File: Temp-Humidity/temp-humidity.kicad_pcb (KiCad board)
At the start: 2 copper layers, 15 parts, among them P1 VIN, P2 GND, P3 NRF24L01, P4 CONN_02X03, P5 SERIAL/DEBUG, U1 NCP1402, U2 AT25DF512, U4 ATSHA204A

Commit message: Update schematics
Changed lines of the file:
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@@
     (links 32)
     (no_connects 32)
-    (area 0 0 0 0)
+    (area 109.80396 75.84508 165.465472 113.247321)
     (thickness 1.6)
-    (drawings 0)
+    (drawings 1)
     (tracks 0)
     (zones 0)
@@
     )
   )
+  (gr_line (start 0 0) (end 100 0) (angle 90) (layer Edge.Cuts) (width 0.15))
 )

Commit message: More work on hum/temp sensor
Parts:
- added C10: 22uF, Capacitors_SMD:C_0805_HandSoldering, B.Cu at (143.9, 102.5)
- added C3: 100uF, Capacitors_SMD:C_0805_HandSoldering, B.Cu at (139.0, 82.2)
- added C4: C_Small, Capacitors_SMD:C_0805_HandSoldering, B.Cu at (147.0, 95.6)
- added C5: 22uF, Capacitors_SMD:C_0805_HandSoldering, B.Cu at (139.0, 84.4)
- added C6: 4u7, Capacitors_SMD:C_0805_HandSoldering, B.Cu at (134.9, 86.6)
- added C7: 12pF, Capacitors_SMD:C_0805_HandSoldering, B.Cu at (132.5, 95.5)
- added C8: 12pF, Capacitors_SMD:C_0805_HandSoldering, B.Cu at (150.5, 83.8)
- added C9: 100nF, Capacitors_SMD:C_0805_HandSoldering, B.Cu at (143.9, 104.8)
- added D1: MBR0520LT1G, Diodes_SMD:SOD-123, F.Cu at (143.5, 79.0)
- added IC1: ATMEGA328P-A, Housings_QFP:TQFP-32_7x7mm_Pitch0.8mm, B.Cu at (139.9, 95.8)
- added JP1: Jumper_NO_Small, Pin_Headers:Pin_Header_Straight_1x02, F.Cu at (130.0, 82.7)
- added R5: 4k7, Resistors_SMD:R_0805_HandSoldering, F.Cu at (144.1, 105.7)
- added R6: 4k7, Resistors_SMD:R_0805_HandSoldering, F.Cu at (130.1, 79.0)
- added R7: 10k, Resistors_SMD:R_0805_HandSoldering, B.Cu at (134.0, 104.9)
- added U3: HDC1080, TO_SOT_Packages_SMD:SC-70-6, F.Cu at (130.0, 108.2)
- added U5: NCP1402, TO_SOT_Packages_SMD:SOT-23-5, F.Cu at (134.1, 83.7)
- added U6: RFM69HW, kicad-libraries:RFM69HW, F.Cu at (139.8, 95.7)
- added Y1: 12MHz, Crystals:Crystal_MC-156, F.Cu at (146.1, 84.1)
- C1, C2, U2: moved to B.Cu
- L1: value INDUCTOR_SMALL -> 47uF
- P1: value VIN -> BATTERY; footprint Pin_Headers:Pin_Header_Straight_1x01 -> Connectors_JST:JST_PH_S2B-PH-K_02x2.00mm_Angled
- P2: value GND -> ANTENNA; footprint Pin_Headers:Pin_Header_Straight_1x01 -> Connect:1pin
- R1: value 4k7 -> 40k2; moved to B.Cu
- R2: value R_Small -> 48k7; moved to B.Cu
- R3: value R_Small -> 4k7; moved to B.Cu
- R4: value 10k -> 4k7; moved to B.Cu
- U1: value NCP1402 -> TPL5110; footprint TO_SOT_Packages_SMD:SOT-23-5 -> TO_SOT_Packages_SMD:SOT-23-6_Handsoldering
- moved P5 32.2 mm to (146.1, 108.8), turned to 270 degrees
- moved P3 31.7 mm to (144.1, 72.6), turned to 270 degrees
- moved P1 31.1 mm to (132.1, 75.2), turned to 180 degrees
- moved C1 29.0 mm to (133.9, 102.5), turned to 180 degrees
- moved P4 26.3 mm to (150.1, 77.7), turned to 180 degrees
- moved R3 24.4 mm to (134.8, 88.7)
- moved U1 23.5 mm to (138.9, 83.8)
- moved U2 23.4 mm to (145.5, 83.9)
- moved C2 21.6 mm to (138.9, 104.9)
- moved R1 17.2 mm to (139.7, 86.6)
- moved U4 14.3 mm to (134.5, 105.4), turned to 90 degrees
- moved P2 12.5 mm to (150.8, 108.5)
- moved R2 11.2 mm to (139.7, 88.7)
- moved R4 8.49 mm to (138.9, 102.5)
- moved L1 1.17 mm to (137.2, 79.3), turned to 180 degrees
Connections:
- C1 pad 1: VDD -> +3V3
- C2 pad 1: VDD -> +3V3
- C2 pad 2: (no net) -> GND
- L1 pad 1: VCC -> +BATT
- P1 pad 1: VCC -> +BATT
- P2 pad 1: GND -> Net-(P2-Pad1)
- P3 pad 3: (no net) -> /CE
- P3 pad 4: (no net) -> /CSN
- P3 pad 8: (no net) -> /IRQ
- P5 pad 1: (no net) -> /DTR
- P5 pad 2: (no net) -> /TX
- P5 pad 3: (no net) -> /RX
- P5 pad 4: +3V3 -> VDD
- R1 pad 1: +3V3 -> Net-(R1-Pad1)
- R1 pad 2: /FLASH_CS -> GND
- R2 pad 1: (no net) -> Net-(R1-Pad1)
- R2 pad 2: +3V3 -> GND
- R3 pad 2: /SDA -> /FLASH_CS
- R4 pad 2: /RESET -> /SCL
- U1 pad 1: +3V3 -> +BATT
- U1 pad 2: +3V3 -> GND
- U1 pad 3: (no net) -> Net-(R1-Pad1)
- U1 pad 4: GND -> /SLEEP
- U1 pad 5: Net-(D1-Pad2) -> Net-(U1-Pad5)

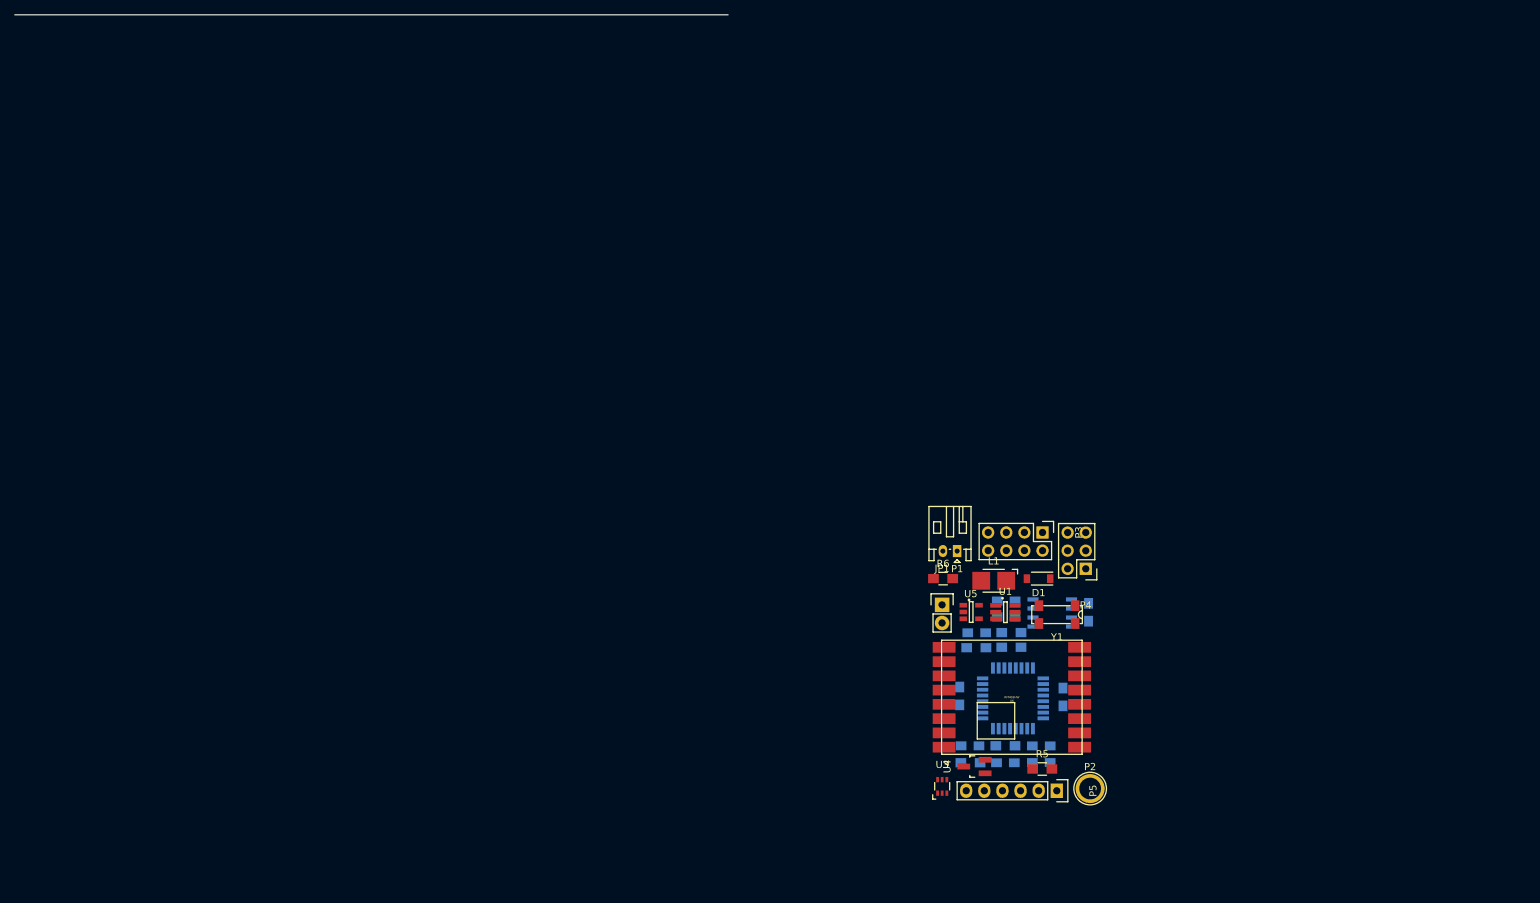
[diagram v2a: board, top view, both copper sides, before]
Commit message: Remove alimentation
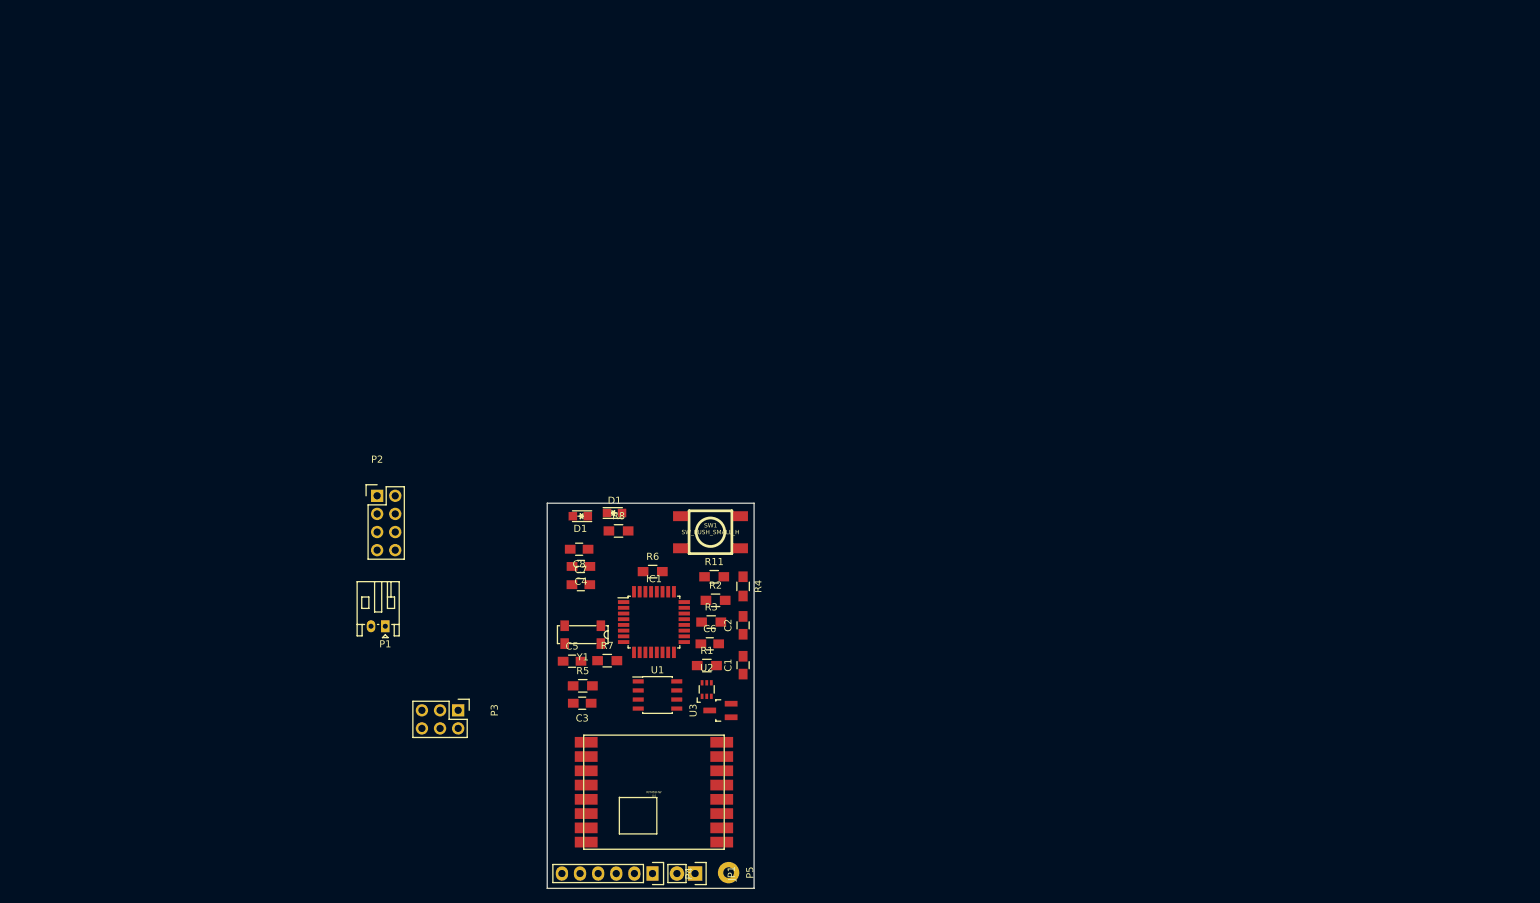
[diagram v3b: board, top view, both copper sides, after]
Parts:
- removed C10: 22uF, Capacitors_SMD:C_0805_HandSoldering
- removed C9: 100nF, Capacitors_SMD:C_0805_HandSoldering
- removed the D1 at (143.5, 79.0)
- removed L1: 47uF, Inductors:Inductor_1212
- removed the U4 at (134.5, 105.4)
- removed U5: NCP1402, TO_SOT_Packages_SMD:SOT-23-5
- added D1: LED, LEDs:LED_0805, F.Cu at (84.1, 69.8)
- added D1: LED, LEDs:LED_0805, F.Cu at (79.3, 70.3)
- added R11: 10k, Resistors_SMD:R_0805_HandSoldering, F.Cu at (98.1, 78.8)
- added R8: 160, Resistors_SMD:R_0805_HandSoldering, F.Cu at (84.6, 72.4)
- added SW1: SW_PUSH_SMALL_H, kicad-libraries:SW_06_SMD, F.Cu at (97.5, 72.5)
- C1, C4, C8, IC1, R4: moved to F.Cu
- C2: value C_Small -> 100uF; moved to F.Cu
- C3: value 100uF -> C_Small; moved to F.Cu
- C5: value 22uF -> 12pF; moved to F.Cu
- C6: value 4u7 -> 12pF; moved to F.Cu
- C7: value 12pF -> 4u7; moved to F.Cu
- P2: value ANTENNA -> NRF24L01; footprint Connect:1pin -> Pin_Headers:Pin_Header_Straight_2x04
- P3: value NRF24L01 -> CONN_02X03; footprint Pin_Headers:Pin_Header_Straight_2x04 -> Pin_Headers:Pin_Header_Straight_2x03
- P4: value CONN_02X03 -> SERIAL/DEBUG; footprint Pin_Headers:Pin_Header_Straight_2x03 -> Pin_Headers:Pin_Header_Straight_1x06
- P5: value SERIAL/DEBUG -> ANTENNA; footprint Pin_Headers:Pin_Header_Straight_1x06 -> Measurement_Points:Measurement_Point_Round-TH_Big
- R1: value 40k2 -> 10k; moved to F.Cu
- R2: value 48k7 -> 160; moved to F.Cu
- R3: value 4k7 -> 10k; moved to F.Cu
- R7: value 10k -> 4k7; moved to F.Cu
- U1: value TPL5110 -> AT25DF512; footprint TO_SOT_Packages_SMD:SOT-23-6_Handsoldering -> Housings_SOIC:SOIC-8_3.9x4.9mm_Pitch1.27mm
- U2: value AT25DF512 -> HDC1080; footprint Housings_SOIC:SOIC-8_3.9x4.9mm_Pitch1.27mm -> TO_SOT_Packages_SMD:SC-70-6; moved to F.Cu
- U3: value HDC1080 -> ATSHA204A; footprint TO_SOT_Packages_SMD:SC-70-6 -> TO_SOT_Packages_SMD:SOT-23_Handsoldering
- moved P2 108.1 mm to (50.8, 67.4)
- moved P3 85.6 mm to (62.2, 97.5)
- moved P1 80.9 mm to (51.9, 85.7)
- moved P4 74.3 mm to (89.4, 120.4), turned to 270 degrees
- moved C8 72.0 mm to (79.1, 74.9), turned to 180 degrees
- moved C4 70.0 mm to (79.4, 77.3), turned to 180 degrees
- moved Y1 66.6 mm to (79.6, 86.9)
- moved R5 65.5 mm to (79.6, 94.1)
- moved C5 61.2 mm to (78.1, 90.6)
- moved C3 61.1 mm to (79.6, 96.5)
- moved C7 55.4 mm to (79.4, 79.9), turned to 0 degrees
- moved R7 52.9 mm to (83.1, 90.6)
- moved U4 51.9 mm to (89.6, 109.0)
- moved IC1 51.5 mm to (89.6, 85.1)
- moved JP1 51.2 mm to (95.4, 120.4), turned to 270 degrees
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- renumbered U6 to U4
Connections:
- C3 pad 1: +BATT -> +3V3
- C5 pad 1: +3V3 -> GND
- C5 pad 2: GND -> Net-(C5-Pad2)
- C6 pad 1: +3V3 -> GND
- C6 pad 2: GND -> Net-(C6-Pad2)
- C7 pad 1: GND -> +3V3
- C7 pad 2: Net-(C7-Pad2) -> GND
- C8 pad 2: Net-(C8-Pad2) -> (no net)
- IC1 pad 1: /SLEEP -> (no net)
- IC1 pad 2: (no net) -> Net-(IC1-Pad2)
- IC1 pad 23: (no net) -> /BTN1
- IC1 pad 7: Net-(C7-Pad2) -> Net-(C5-Pad2)
- IC1 pad 8: Net-(C8-Pad2) -> Net-(C6-Pad2)
- P1 pad 1: +BATT -> +3V3
- P2 pad 1: Net-(P2-Pad1) -> GND
- P3 pad 1: GND -> /MISO
- P3 pad 3: /CE -> /SCK
- P3 pad 4: /CSN -> /MOSI
- P3 pad 5: /SCK -> /RESET
- P3 pad 6: /MOSI -> GND
- P4 pad 1: /MISO -> /DTR
- P4 pad 2: +3V3 -> /TX
- P4 pad 3: /SCK -> /RX
- P4 pad 4: /MOSI -> VDD
- P4 pad 5: /RESET -> GND
- P5 pad 1: /DTR -> Net-(P5-Pad1)
- R1 pad 1: Net-(R1-Pad1) -> /BTN1
- R2 pad 1: Net-(R1-Pad1) -> Net-(D1-Pad1)
- R2 pad 2: GND -> Net-(IC1-Pad2)
- R3 pad 2: /FLASH_CS -> /DTR
- R4 pad 2: /SCL -> /FLASH_CS
- R5 pad 2: /SDA -> /SCL
- R6 pad 2: /RESET -> /SDA
- R7 pad 2: /DTR -> /RESET
- U1 pad 1: +BATT -> /FLASH_CS
- U1 pad 2: GND -> /MISO
- U1 pad 3: Net-(R1-Pad1) -> +3V3
- U1 pad 4: /SLEEP -> GND
- U1 pad 5: Net-(U1-Pad5) -> /MOSI
- U1 pad 6: +BATT -> /SCK
- U2 pad 1: /FLASH_CS -> /SDA
- U2 pad 2: /MISO -> GND
- U2 pad 3: +3V3 -> (no net)
- U2 pad 4: GND -> (no net)
- U2 pad 5: /MOSI -> +3V3
- U2 pad 6: /SCK -> /SCL
- U3 pad 2: GND -> +3V3
- U3 pad 3: (no net) -> GND
- U4 pad 7: Net-(P2-Pad1) -> Net-(P5-Pad1)
- Y1 pad 1: Net-(C7-Pad2) -> Net-(C5-Pad2)
- Y1 pad 2: Net-(C8-Pad2) -> Net-(C6-Pad2)
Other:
- board outline added: 29 x 54 mm

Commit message: More work on pcb, but bad cutting edges
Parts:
- removed the C5 at (78.1, 90.6)
- removed the C6 at (97.4, 88.2)
- removed the D1 at (84.1, 69.8)
- removed the D1 at (79.3, 70.3)
- removed P5: ANTENNA, Measurement_Points:Measurement_Point_Round-TH_Big
- removed the R1 at (97.0, 91.2)
- removed the R2 at (98.2, 82.1)
- added C7: 4u7, Capacitors_SMD:C_0805_HandSoldering, F.Cu at (200.4, 62.2)
- added D1: LED, LEDs:LED_0805, F.Cu at (198.3, 33.7)
- added U5: RFM69HW, mysensors_radios:RFM69HW_SMD, F.Cu at (189.1, 61.1)
- C2: renamed from C3; value C_Small -> 100uF
- C3: renamed from C2; value 100uF -> C_Small
- C5: renamed from C7; value 4u7 -> 12pF
- P1: moved to B.Cu
- P2: value NRF24L01 -> CONN_02X03; footprint Pin_Headers:Pin_Header_Straight_2x04 -> Pin_Headers:Pin_Header_Straight_2x03
- P3: value CONN_02X03 -> SERIAL/DEBUG; footprint Pin_Headers:Pin_Header_Straight_2x03 -> Pin_Headers:Pin_Header_Straight_1x06
- P4: value SERIAL/DEBUG -> ANTENNA; footprint Pin_Headers:Pin_Header_Straight_1x06 -> Measurement_Points:Measurement_Point_Round-TH_Big
- R3: renamed from R7; value 4k7 -> 10k
- R4: renamed from R3; value 10k -> 4k7
- U4: value RFM69HW -> NRF24L01; footprint kicad-libraries:RFM69HW -> mysensors_radios:NRF24L01-SMD
- Y1: footprint Crystals:Crystal_MC-156 -> Crystals:Crystal_SMD_5032_2Pads
- moved P1 168.2 mm to (210.3, 29.1)
- moved P2 157.0 mm to (205.5, 41.0)
- moved C2 135.7 mm to (198.3, 30.9), turned to 0 degrees
- moved P3 133.7 mm to (184.7, 44.0), turned to 0 degrees
- moved U1 122.5 mm to (205.8, 55.2)
- moved Y1 121.7 mm to (196.6, 53.3), turned to 0 degrees
- moved C6 121.6 mm to (199.3, 57.0), turned to 0 degrees
- moved U3 120.8 mm to (203.1, 36.4), turned to 0 degrees
- moved R7 120.3 mm to (206.2, 49.0), turned to 180 degrees
- moved C4 120.2 mm to (191.5, 34.0)
- moved R2 119.4 mm to (198.4, 36.0), turned to 180 degrees
- moved C5 117.2 mm to (194.3, 56.9), turned to 180 degrees
- moved R6 117.1 mm to (189.3, 53.1), turned to 90 degrees
- moved IC1 115.1 mm to (197.4, 44.6)
- moved R3 114.8 mm to (188.4, 45.0), turned to 90 degrees
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- renumbered C8 to C6, R11 to R1, R8 to R2, R4 to R5, R5 to R6, R6 to R7
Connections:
- C5 pad 1: +3V3 -> GND
- C5 pad 2: GND -> Net-(C5-Pad2)
- C6 pad 2: (no net) -> Net-(C6-Pad2)
- P1 pad 1: +3V3 -> GND
- P1 pad 2: GND -> +3V3
- P2 pad 1: GND -> /MISO
- P2 pad 3: /CE -> /SCK
- P2 pad 4: /CSN -> /MOSI
- P2 pad 5: /SCK -> /RESET
- P2 pad 6: /MOSI -> GND
- P3 pad 1: /MISO -> /DTR
- P3 pad 2: +3V3 -> /TX
- P3 pad 3: /SCK -> /RX
- P3 pad 4: /MOSI -> VDD
- P3 pad 5: /RESET -> GND
- P4 pad 1: /DTR -> Net-(P4-Pad1)
- R2 pad 1: (no net) -> Net-(D1-Pad1)
- R3 pad 2: /RESET -> /DTR
- R4 pad 2: /DTR -> /FLASH_CS
- R5 pad 2: /FLASH_CS -> /SCL
- R6 pad 2: /SCL -> /SDA
- R7 pad 2: /SDA -> /RESET
- U4 pad 1: (no net) -> GND
- U4 pad 2: /CSN -> +3V3
- U4 pad 3: /MOSI -> /CE
- U4 pad 4: /MISO -> /CSN
- U4 pad 6: GND -> /MOSI
- U4 pad 7: Net-(P5-Pad1) -> /MISO
- U4 pad 8: GND -> /IRQ
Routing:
- added copper zone on F.Cu, net +3V3
- added copper zone on B.Cu, net GND
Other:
- board size 29 x 54 mm -> 54 x 29 mm
